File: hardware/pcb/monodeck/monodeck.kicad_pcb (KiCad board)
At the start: 2 copper layers, 72 x 54.8 mm, 14 parts, among them J1 Conn_01x20_Socket, J2 Conn_01x20_Socket, U1 TP4056

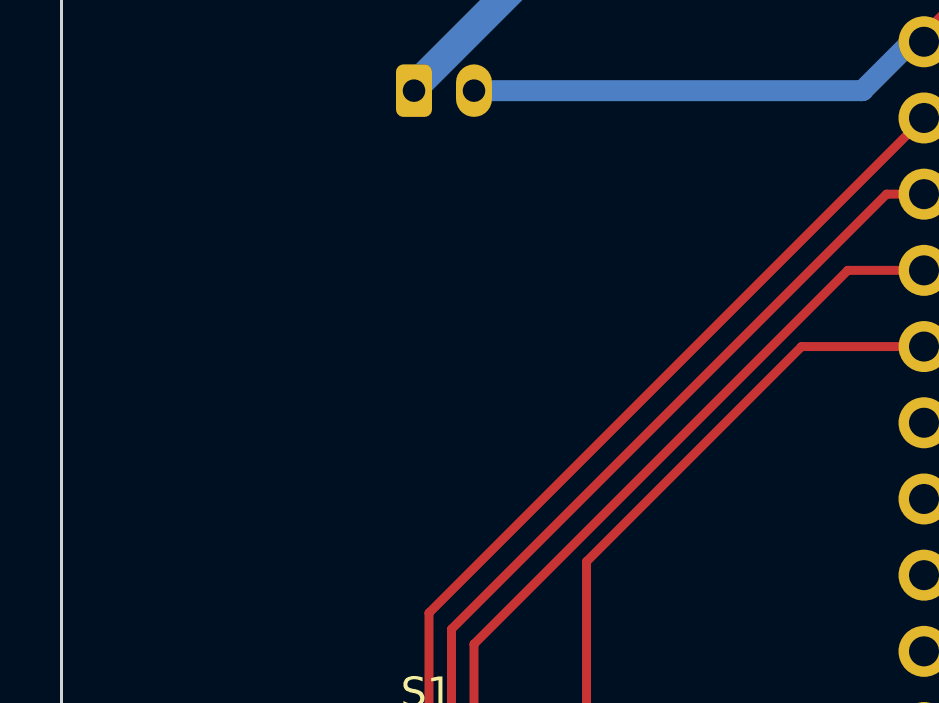
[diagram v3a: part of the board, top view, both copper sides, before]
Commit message: added monodeck logo on pcb
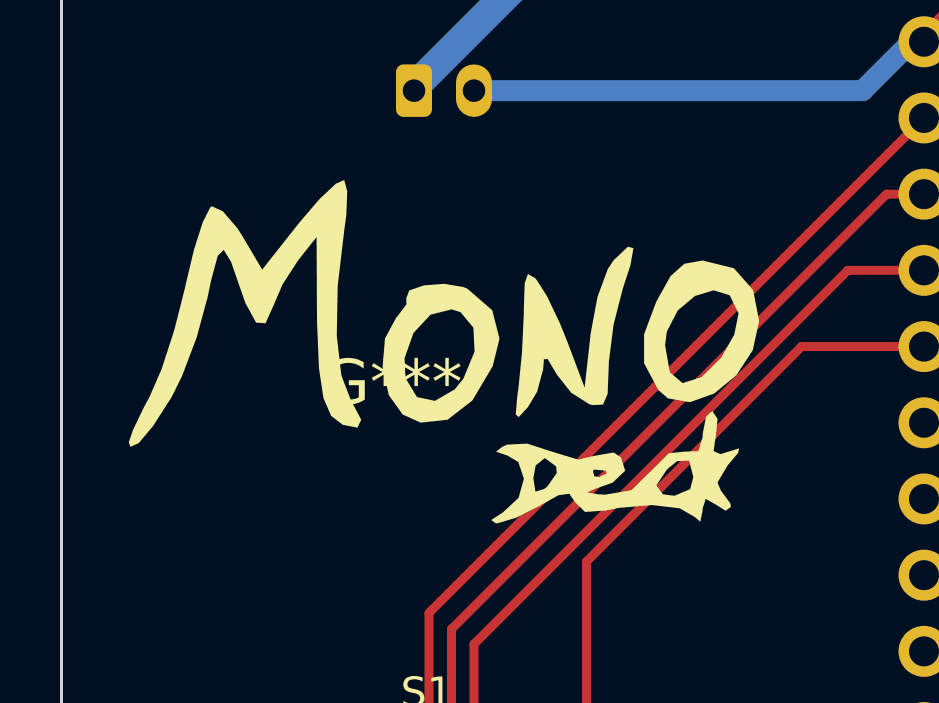
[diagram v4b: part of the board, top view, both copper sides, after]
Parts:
- added G***: LOGO, LOGO, F.Cu at (139.8, 71.3)
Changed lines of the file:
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@@
+		(embedded_fonts no)
+	)
+	(footprint "LOGO"
+		(layer "F.Cu")
+		(at 139.77531 71.290622)
+		(property "Reference" "G***"
+			(at 0 0 0)
+			(layer "F.SilkS")
+			(effects
+				(font
+					(size 1.5 1.5)
+					(thickness 0.3)
+				)
+			)
+		)
+		(property "Value" "LOGO"
+			(at 0.75 0 0)
+			(layer "F.SilkS")
+			(hide yes)
+			(effects
+				(font
+					(size 1.5 1.5)
+					(thickness 0.3)
+				)
+			)
+		)
+		(property "Datasheet" ""
+			(at 0 0 0)
+			(layer "F.Fab")
+			(hide yes)
+			(effects
+				(font
+					(size 1.27 1.27)
+					(thickness 0.15)
+				)
+			)
+		)
+		(property "Description" ""
+			(at 0 0 0)
+			(layer "F.Fab")
+			(hide yes)
+			(effects
+				(font
+					(size 1.27 1.27)
+					(thickness 0.15)
+				)
+			)
+		)
+		(attr board_only exclude_from_pos_files exclude_from_bom)
+		(fp_poly
+			(pts
+				(xy 11.386807 -3.82187) (xy 12.029106 -3.095544) (xy 12.229629 -2.061663) (xy 12.017494 -1.089785)
+				(xy 11.47172 -0.252942) (xy 10.728255 0.355999) (xy 9.923044 0.64417) (xy 9.192034 0.518704) (xy 8.867321 0.235185)
+				(xy 8.393867 -0.656473) (xy 8.393299 -1.257984) (xy 9.093826 -1.257984) (xy 9.251943 -0.353571)
+				(xy 9.678906 0.008079) (xy 10.303633 -0.188748) (xy 10.966493 -0.843968) (xy 11.399966 -1.607484)
+				(xy 11.541382 -2.301834) (xy 11.538018 -2.330271) (xy 11.248116 -2.919066) (xy 10.714688 -3.085207)
+				(xy 10.087634 -2.894457) (xy 9.516849 -2.412575) (xy 9.152232 -1.705324) (xy 9.093826 -1.257984)
+				(xy 8.393299 -1.257984) (xy 8.39296 -1.616412) (xy 8.80134 -2.709007) (xy 9.281071 -3.565231) (xy 9.737755 -3.971806)
+				(xy 10.339149 -4.076514) (xy 10.353722 -4.076544)
+			)
+			(stroke
+				(width 0)
+				(type solid)
+			)
+			(fill yes)
+			(layer "F.SilkS")
+		)
+		(fp_poly
+			(pts
+				(xy 2.376156 -3.19426) (xy 2.507889 -3.136206) (xy 3.332499 -2.421344) (xy 3.574868 -1.474746) (xy 3.348367 -0.555927)
+				(xy 2.669436 0.587817) (xy 1.841859 1.230139) (xy 0.949682 1.325861) (xy 0.349579 1.056093) (xy -0.117637 0.405971)
+				(xy -0.320736 -0.530776) (xy -0.296864 -0.823618) (xy 0.410037 -0.823618) (xy 0.441776 -0.159075)
+				(xy 0.824155 0.472919) (xy 1.423051 0.599066) (xy 2.081989 0.217709) (xy 2.368808 -0.138661) (xy 2.74434 -1.044755)
+				(xy 2.704249 -1.840348) (xy 2.277089 -2.355865) (xy 1.979694 -2.44946) (xy 1.275701 -2.272348) (xy 0.708449 -1.664823)
+				(xy 0.410037 -0.823618) (xy -0.296864 -0.823618) (xy -0.243241 -1.481425) (xy 0.131325 -2.173252)
+				(xy 0.153337 -2.192197) (xy 0.472697 -2.619144) (xy 0.469084 -2.824303) (xy 0.565685 -3.08135) (xy 1.064323 -3.251424)
+				(xy 1.74211 -3.300427)
+			)
+			(stroke
+				(width 0)
+				(type solid)
+			)
+			(fill yes)
+			(layer "F.SilkS")
+		)
+		(fp_poly
+			(pts
+				(xy 8.039382 -4.490887) (xy 7.939405 -3.921439) (xy 7.686064 -3.145293) (xy 7.378183 -1.948445)
+				(xy 7.218561 -0.694668) (xy 7.212345 -0.460303) (xy 7.178768 0.372319) (xy 7.025652 0.723958) (xy 6.674419 0.739452)
+				(xy 6.574584 0.715247) (xy 5.963577 0.328625) (xy 5.489608 -0.274531) (xy 5.178816 -0.795402) (xy 5.054157 -0.786202)
+				(xy 5.029838 -0.45191) (xy 4.826003 0.300253) (xy 4.524833 0.802411) (xy 4.220558 1.138297) (xy 4.114834 1.055756)
+				(xy 4.165229 0.468374) (xy 4.207801 0.15679) (xy 4.323681 -1.010887) (xy 4.3843 -2.280186) (xy 4.386672 -2.497443)
+				(xy 4.414892 -3.326606) (xy 4.523235 -3.627031) (xy 4.755546 -3.496091) (xy 4.810295 -3.438184)
+				(xy 5.159036 -2.888981) (xy 5.585873 -1.993316) (xy 5.821154 -1.411112) (xy 6.41184 0.15679) (xy 6.614827 -1.655275)
+				(xy 6.841092 -2.865431) (xy 7.186214 -3.799034) (xy 7.379 -4.087445) (xy 7.855303 -4.537867)
+			)
+			(stroke
+				(width 0)
+				(type solid)
+			)
+			(fill yes)
+			(layer "F.SilkS")
+		)
+		(fp_poly
+			(pts
+				(xy -1.501638 -6.390104) (xy -1.529357 -5.61593) (xy -1.597227 -5.10685) (xy -1.818553 -3.232688)
+				(xy -1.849496 -1.56764) (xy -1.695157 -0.244677) (xy -1.379127 0.577665) (xy -1.032674 1.228605)
+				(xy -1.160739 1.494136) (xy -1.648909 1.3968) (xy -2.036641 1.101932) (xy -2.294329 0.504852) (xy -2.44367 -0.492697)
+				(xy -2.506362 -1.988969) (xy -2.511334 -2.508643) (xy -2.522588 -4.860494) (xy -3.143709 -4.076544)
+				(xy -3.657092 -3.280545) (xy -3.954682 -2.587038) (xy -4.224327 -1.986472) (xy -4.538327 -2.008634)
+				(xy -4.89108 -2.651082) (xy -5.034143 -3.057408) (xy -5.3744 -4.036787) (xy -5.616162 -4.432935)
+				(xy -5.816744 -4.235486) (xy -6.033461 -3.434076) (xy -6.155397 -2.854637) (xy -6.513264 -1.533121)
+				(xy -7.007441 -0.22427) (xy -7.358556 0.480605) (xy -7.969944 1.433334) (xy -8.448745 2.006602)
+				(xy -8.731326 2.133581) (xy -8.780248 1.973739) (xy -8.639921 1.563828) (xy -8.285822 0.830369)
+				(xy -8.090392 0.465726) (xy -7.687782 -0.463694) (xy -7.268681 -1.750312) (xy -6.9173 -3.132303)
+				(xy -6.887081 -3.27559) (xy -6.606752 -4.447901) (xy -6.316563 -5.356494) (xy -6.06841 -5.846287)
+				(xy -6.013081 -5.88741) (xy -5.645676 -5.718993) (xy -5.160348 -5.152526) (xy -4.994082 -4.891591)
+				(xy -4.335626 -3.775591) (xy -3.093828 -5.346584) (xy -2.419545 -6.131972) (xy -1.877588 -6.640916)
+				(xy -1.601194 -6.762552)
+			)
+			(stroke
+				(width 0)
+				(type solid)
+			)
+			(fill yes)
+			(layer "F.SilkS")
+		)
+		(fp_poly
+			(pts
+				(xy 10.845237 1.198742) (xy 10.789608 1.728235) (xy 10.710518 2.278576) (xy 10.943933 2.373714)
+				(xy 11.175609 2.302224) (xy 11.564784 2.183221) (xy 11.528637 2.338337) (xy 11.190066 2.737918)
+				(xy 10.841721 3.318739) (xy 10.95488 3.593547) (xy 11.27246 4.020211) (xy 11.288888 4.133445) (xy 11.111601 4.263263)
+				(xy 10.818518 4.076543) (xy 10.449023 3.867352) (xy 10.344879 4.192872) (xy 10.343346 4.273332)
+				(xy 10.266064 4.630333) (xy 10.095844 4.478534) (xy 9.582026 4.181229) (xy 8.664513 4.072635) (xy 7.542296 4.167966)
+				(xy 7.13785 4.252358) (xy 6.42675 4.302428) (xy 6.092947 3.975843) (xy 5.901568 3.696136) (xy 5.543799 3.744883)
+				(xy 4.913121 4.09565) (xy 4.130953 4.494066) (xy 3.510977 4.679524) (xy 3.449382 4.681308) (xy 3.296898 4.57139)
+				(xy 3.684567 4.32098) (xy 4.210262 3.832597) (xy 4.38864 3.192652) (xy 4.38239 3.174198) (xy 4.703703 3.174198)
+				(xy 4.77289 3.626856) (xy 5.065691 3.535847) (xy 5.170621 3.452248) (xy 5.480959 3.010583) (xy 5.475243 2.926748)
+				(xy 6.689711 2.926748) (xy 6.732756 3.113171) (xy 6.898765 3.135802) (xy 7.156877 3.021068) (xy 7.107818 2.926748)
+				(xy 6.735672 2.889219) (xy 6.689711 2.926748) (xy 5.475243 2.926748) (xy 5.465694 2.786691) (xy 5.087181 2.506976)
+				(xy 4.780093 2.753703) (xy 4.703703 3.174198) (xy 4.38239 3.174198) (xy 4.200258 2.636467) (xy 3.841357 2.423373)
+				(xy 3.460137 2.2939) (xy 3.669552 2.129147) (xy 3.829367 2.057852) (xy 4.502065 2.025224) (xy 5.279293 2.279123)
+				(xy 6.200567 2.558552) (xy 6.732616 2.432367) (xy 7.378068 2.321283) (xy 7.618863 2.476147) (xy 7.766219 2.926161)
+				(xy 7.346597 3.326348) (xy 6.741975 3.539359) (xy 6.499874 3.649917) (xy 6.881292 3.716009) (xy 7.097885 3.726587)
+				(xy 7.982339 3.576352) (xy 8.14113 3.418751) (xy 8.803235 3.418751) (xy 9.020264 3.714187) (xy 9.407407 3.762962)
+				(xy 9.931496 3.541228) (xy 10.034567 3.135802) (xy 9.894174 2.589863) (xy 9.49559 2.608601) (xy 9.156543 2.884938)
+				(xy 8.803235 3.418751) (xy 8.14113 3.418751) (xy 8.614021 2.949402) (xy 9.222913 2.342371) (xy 9.747617 2.292885)
+				(xy 10.205581 2.277213) (xy 10.346511 1.801763) (xy 10.348147 1.695333) (xy 10.461382 1.120248)
+				(xy 10.667702 0.94074)
+			)
+			(stroke
+				(width 0)
+				(type solid)
+			)
+			(fill yes)
+			(layer "F.SilkS")
+		)
 		(embedded_fonts no)
 	)

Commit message: update: edited gnd plane to connect all gnd nets
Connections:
- J1 pad 19: /GPIO14 -> unconnected-(J1-GP14-Pad19)
- J1 pad 20: /GPIO15 -> unconnected-(J1-GP15-Pad20)
- J1 pad 3: GND1 -> GND
- J2 pad 18: GND2 -> GND
- S1 pad 1: GND1 -> GND
- S2 pad 1: GND1 -> GND
- S2 pad 2: GND1 -> GND
- S3 pad 1: GND1 -> GND
- S4 pad 2: GND1 -> GND
- S5 pad 4: GND2 -> GND
- S6 pad 4: GND2 -> GND
- S7 pad 2: GND2 -> GND
- S8 pad 2: GND2 -> GND
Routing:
- net GND: track 70.7 -> 174.1 mm
- net GND2: track 59.6 -> 0.00 mm
- net GND1: track 43.8 -> 0.00 mm

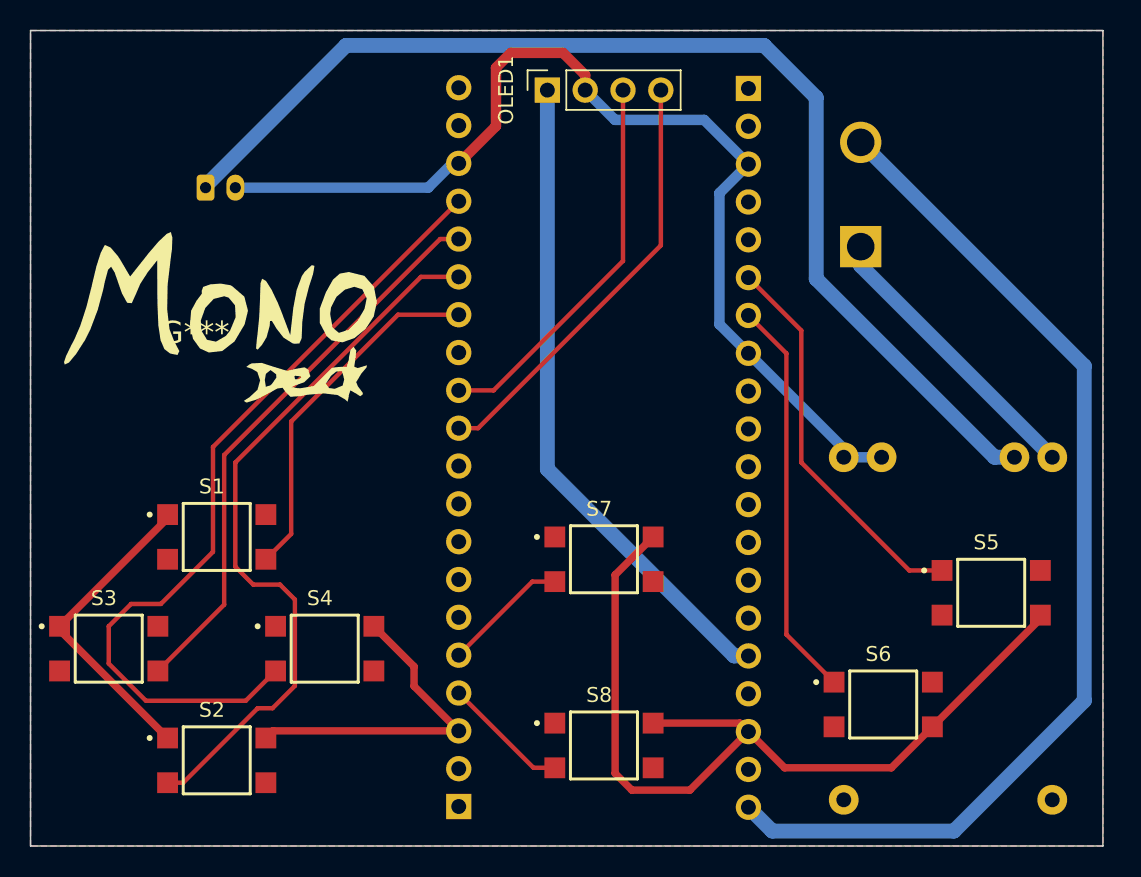
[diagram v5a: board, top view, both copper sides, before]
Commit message: removed redundant traces
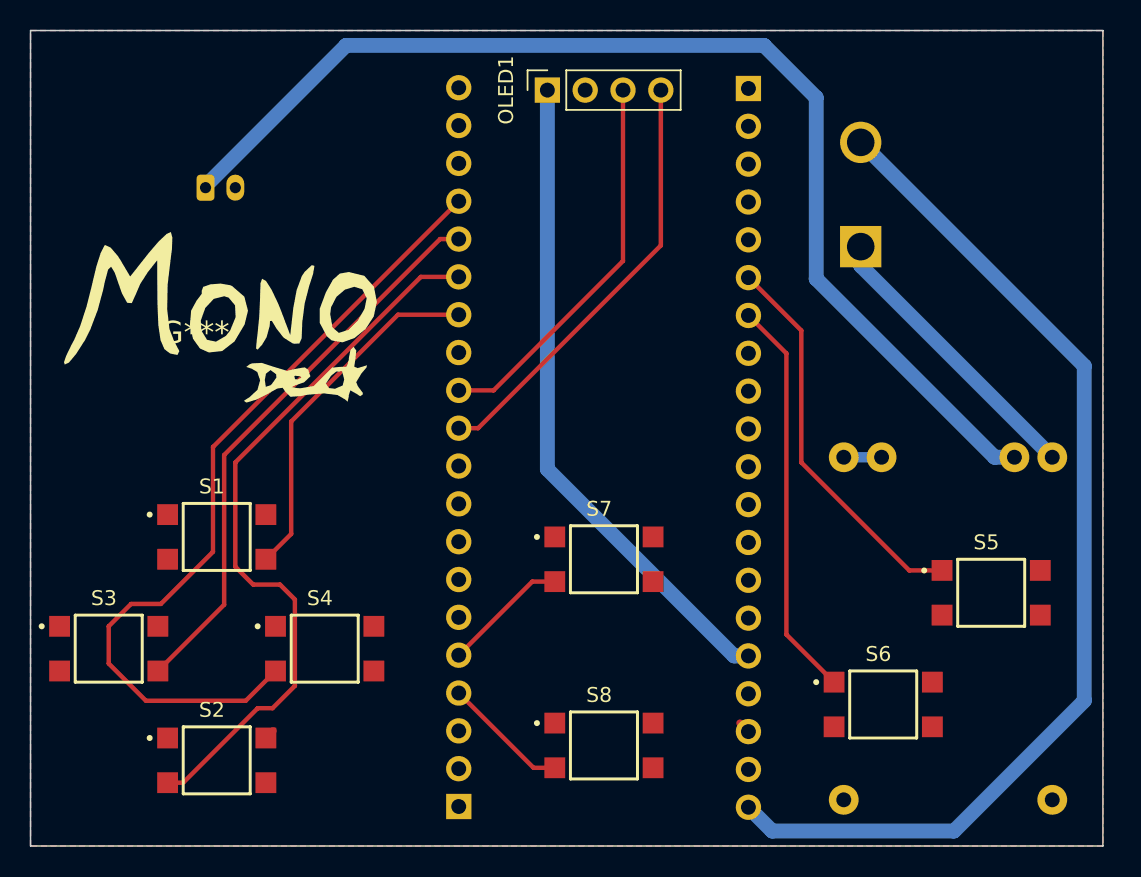
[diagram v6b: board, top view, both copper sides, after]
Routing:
- net GND: track 174.1 -> 6.07 mm
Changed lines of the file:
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@@
-	)
-	(segment
-		(start 189.3 97.75)
-		(end 186.55 100.5)
-		(width 0.5)
-		(layer "F.Cu")
-		(net 1)
-	)
-	(segment
-		(start 168 100.876)
-		(end 169.124 102)
-		(width 0.5)
-		(layer "F.Cu")
-		(net 1)
-	)
-	(segment
-		(start 196.55 90.5)
-		(end 189.3 97.75)
-		(width 0.5)
-		(layer "F.Cu")
-		(net 1)
-	)
-	(segment
-		(start 161 52.5)
-		(end 164.5 52.5)
-		(width 0.7)
-		(layer "F.Cu")
-		(net 1)
-	)
-	(segment
-		(start 157.5 59.92)
-		(end 160 57.42)
-		(width 0.7)
-		(layer "F.Cu")
-		(net 1)
 	)
 	(segment
@@
 	)
 	(segment
-		(start 186.55 100.5)
-		(end 179.38 100.5)
-		(width 0.5)
-		(layer "F.Cu")
-		(net 1)
-	)
-	(segment
-		(start 160 53.5)
-		(end 161 52.5)
-		(width 0.7)
-		(layer "F.Cu")
-		(net 1)
-	)
-	(segment
-		(start 170.55 85)
-		(end 168 87.55)
-		(width 0.5)
-		(layer "F.Cu")
-		(net 1)
-	)
-	(segment
-		(start 169.124 102)
-		(end 173.02 102)
-		(width 0.5)
-		(layer "F.Cu")
-		(net 1)
-	)
-	(segment
-		(start 179.38 100.5)
-		(end 176.95 98.07)
-		(width 0.5)
-		(layer "F.Cu")
-		(net 1)
-	)
-	(segment
-		(start 170.55 97.5)
-		(end 176.38 97.5)
-		(width 0.5)
-		(layer "F.Cu")
-		(net 1)
-	)
-	(segment
-		(start 157.5 98.02)
-		(end 145.03 98.02)
-		(width 0.5)
-		(layer "F.Cu")
-		(net 1)
-	)
-	(segment
 		(start 130.7 91)
 		(end 130.7 91.25)
-		(width 0.5)
-		(layer "F.Cu")
-		(net 1)
-	)
-	(segment
-		(start 130.7 91.25)
-		(end 137.95 98.5)
-		(width 0.5)
-		(layer "F.Cu")
-		(net 1)
-	)
-	(segment
-		(start 160 57.42)
-		(end 160 53.5)
-		(width 0.7)
-		(layer "F.Cu")
-		(net 1)
-	)
-	(segment
-		(start 164.5 52.5)
-		(end 165.99 53.99)
-		(width 0.7)
-		(layer "F.Cu")
-		(net 1)
-	)
-	(segment
-		(start 173.02 102)
-		(end 176.95 98.07)
 		(width 0.5)
 		(layer "F.Cu")
@@
 	)
 	(segment
-		(start 154.5 95.02)
-		(end 154.5 93.7)
-		(width 0.5)
-		(layer "F.Cu")
-		(net 1)
-	)
-	(segment
-		(start 137.95 83.75)
-		(end 130.7 91)
-		(width 0.5)
-		(layer "F.Cu")
-		(net 1)
-	)
-	(segment
-		(start 165.99 53.99)
-		(end 165.99 55)
-		(width 0.7)
-		(layer "F.Cu")
-		(net 1)
-	)
-	(segment
-		(start 154.5 93.7)
-		(end 151.8 91)
-		(width 0.5)
-		(layer "F.Cu")
-		(net 1)
-	)
-	(segment
 		(start 196.55 90.25)
 		(end 196.55 90.5)
@@
 	)
 	(segment
-		(start 157.5 98.02)
-		(end 154.5 95.02)
-		(width 0.5)
-		(layer "F.Cu")
-		(net 1)
-	)
-	(segment
-		(start 168 87.55)
-		(end 168 100.876)
-		(width 0.5)
-		(layer "F.Cu")
-		(net 1)
-	)
-	(segment
-		(start 167.99 57)
-		(end 173.98 57)
-		(width 0.7)
-		(layer "B.Cu")
-		(net 1)
-	)
-	(segment
 		(start 142.5 61.55)
 		(end 142.5 61.5)
 		(width 1)
-		(layer "B.Cu")
-		(net 1)
-	)
-	(segment
-		(start 175 70.72)
-		(end 175 61.92)
-		(width 0.7)
-		(layer "B.Cu")
-		(net 1)
-	)
-	(segment
-		(start 175 61.92)
-		(end 176.95 59.97)
-		(width 0.7)
 		(layer "B.Cu")
 		(net 1)
@@
 	)
 	(segment
-		(start 157.08 59.92)
-		(end 155.45 61.55)
-		(width 0.7)
-		(layer "B.Cu")
-		(net 1)
-	)
-	(segment
-		(start 173.98 57)
-		(end 176.95 59.97)
-		(width 0.7)
-		(layer "B.Cu")
-		(net 1)
-	)
-	(segment
-		(start 155.45 61.55)
-		(end 142.5 61.55)
-		(width 0.7)
-		(layer "B.Cu")
-		(net 1)
-	)
-	(segment
-		(start 183.35 79.07)
-		(end 176.95 72.67)
-		(width 0.7)
-		(layer "B.Cu")
-		(net 1)
-	)
-	(segment
-		(start 165.99 55)
-		(end 167.99 57)
-		(width 0.7)
-		(layer "B.Cu")
-		(net 1)
-	)
-	(segment
 		(start 183.35 79.65)
 		(end 183.35 79.07)
 		(width 0.7)
 		(layer "B.Cu")
-		(net 1)
-	)
-	(segment
-		(start 176.95 72.67)
-		(end 175 70.72)
-		(width 0.7)
-		(layer "B.Cu")
